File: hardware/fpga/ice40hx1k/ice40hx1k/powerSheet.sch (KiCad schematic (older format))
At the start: 6 parts, among them U1 LTC3406ES5

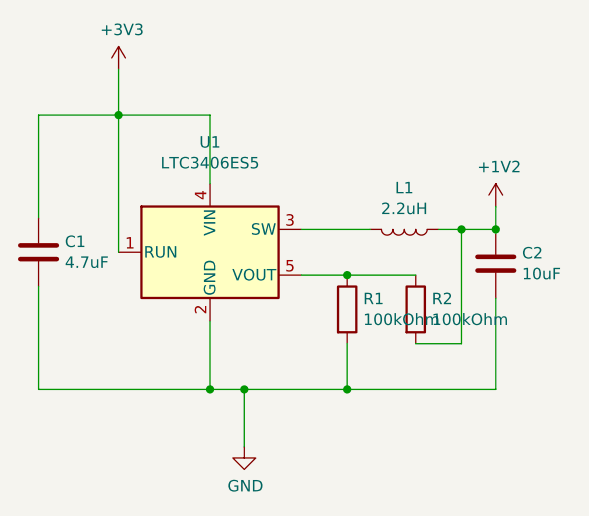
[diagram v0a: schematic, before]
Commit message: std FPGA skeleton
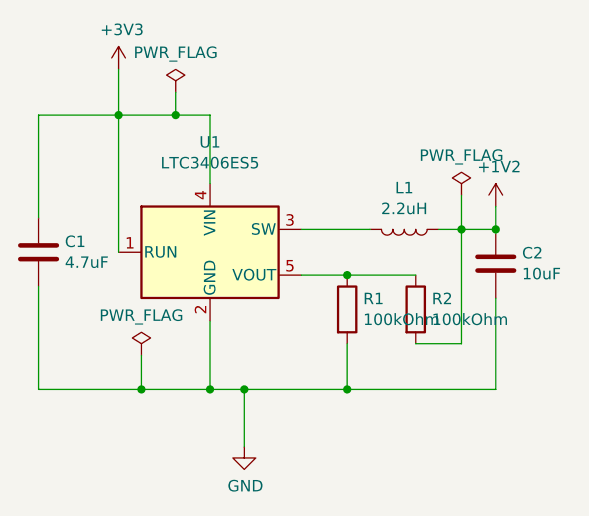
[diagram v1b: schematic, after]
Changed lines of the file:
@@
 	1850 2200 1850 1900
 Wire Wire Line
-	1850 1900 1450 1900
+	1850 1900 1700 1900
 Wire Wire Line
 	1450 1900 1450 2500
@@
 	1100 2650 1100 3100
 Wire Wire Line
-	1100 3100 1850 3100
+	1100 3100 1550 3100
 Wire Wire Line
 	2450 3100 2450 2900
@@
 Wire Wire Line
 	1450 1700 1450 1900
+$Comp
+L power:PWR_FLAG #FLG01
+U 1 1 5EB25836
+P 2950 2250
+F 0 "#FLG01" H 2950 2325 50  0001 C CNN
+F 1 "PWR_FLAG" H 2950 2423 50  0000 C CNN
+F 2 "" H 2950 2250 50  0001 C CNN
+F 3 "~" H 2950 2250 50  0001 C CNN
+	1    2950 2250
+	1    0    0    -1
+$EndComp
+Wire Wire Line
+	2950 2250 2950 2400
+$Comp
+L power:PWR_FLAG #FLG02
+U 1 1 5EB2706F
+P 1700 1800
+F 0 "#FLG02" H 1700 1875 50  0001 C CNN
+F 1 "PWR_FLAG" H 1700 1973 50  0000 C CNN
+F 2 "" H 1700 1800 50  0001 C CNN
+F 3 "~" H 1700 1800 50  0001 C CNN
+	1    1700 1800
+	1    0    0    -1
+$EndComp
+Wire Wire Line
+	1700 1800 1700 1900
+Connection ~ 1700 1900
+Wire Wire Line
+	1700 1900 1450 1900
+$Comp
+L power:PWR_FLAG #FLG03
+U 1 1 5EB2A60C
+P 1550 2950
+F 0 "#FLG03" H 1550 3025 50  0001 C CNN
+F 1 "PWR_FLAG" H 1550 3123 50  0000 C CNN
+F 2 "" H 1550 2950 50  0001 C CNN
+F 3 "~" H 1550 2950 50  0001 C CNN
+	1    1550 2950
+	1    0    0    -1
+$EndComp
+Wire Wire Line
+	1550 2950 1550 3100
+Connection ~ 1550 3100
+Wire Wire Line
+	1550 3100 1850 3100
 $EndSCHEMATC
